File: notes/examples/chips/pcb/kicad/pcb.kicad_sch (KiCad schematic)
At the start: 12 parts, among them J1 BOOT, J2 UART, SW1 BOOT, SW2 USER, U1 STM32F103C8Tx, U2 AMS1117-3.3

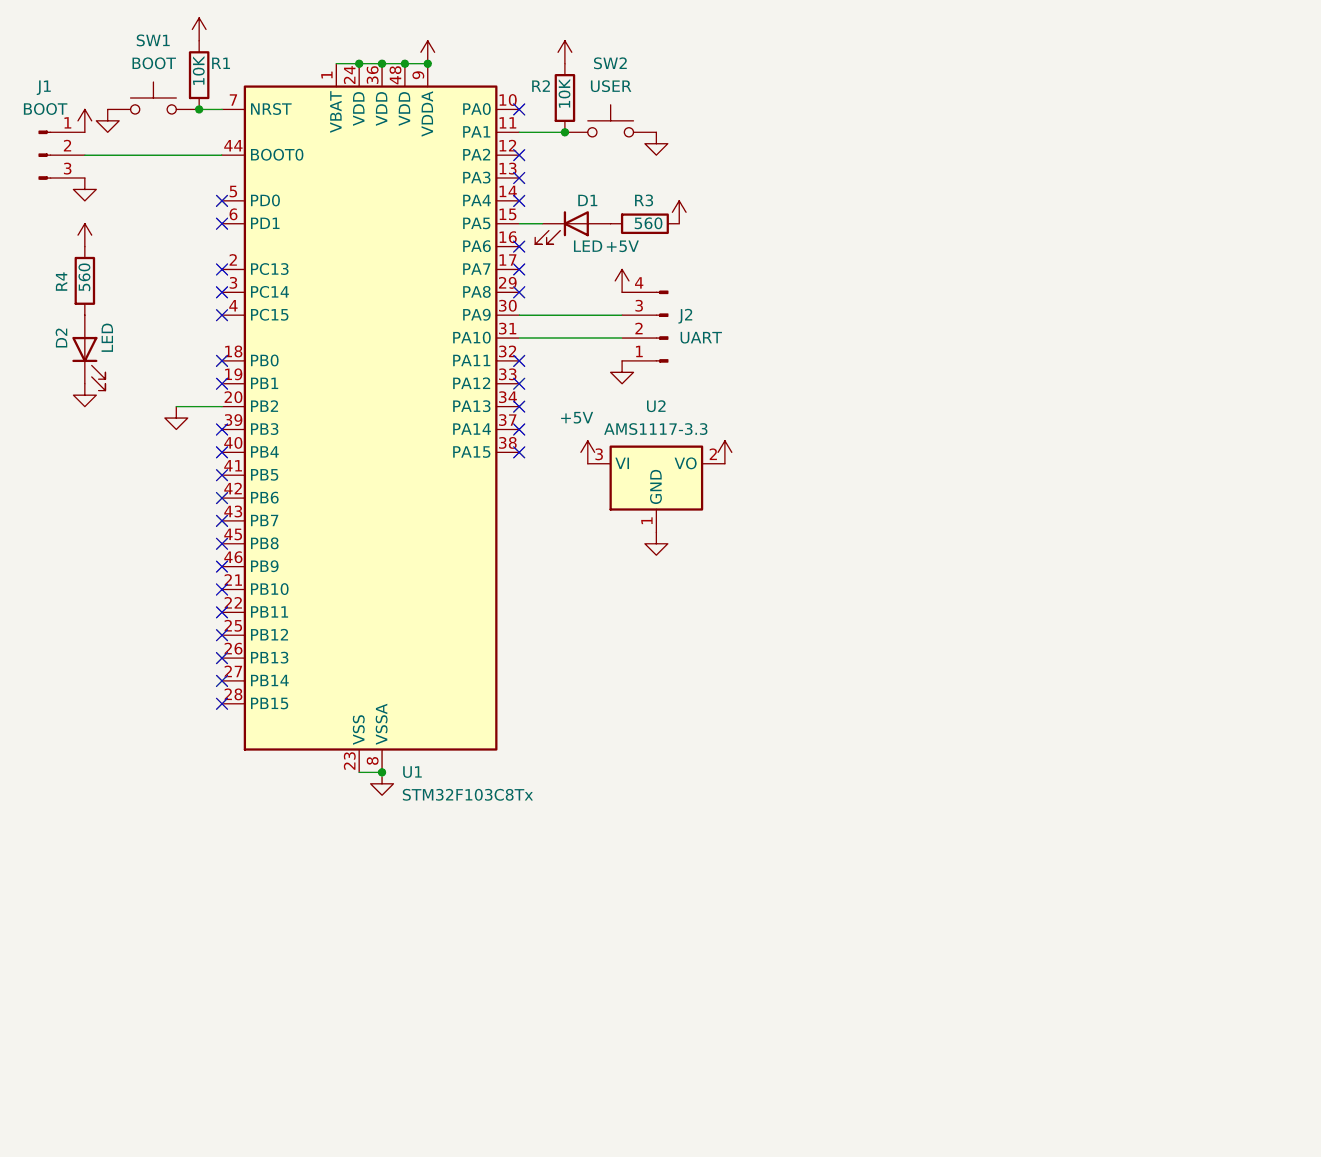
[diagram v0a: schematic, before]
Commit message: Rework KiCAD Guide
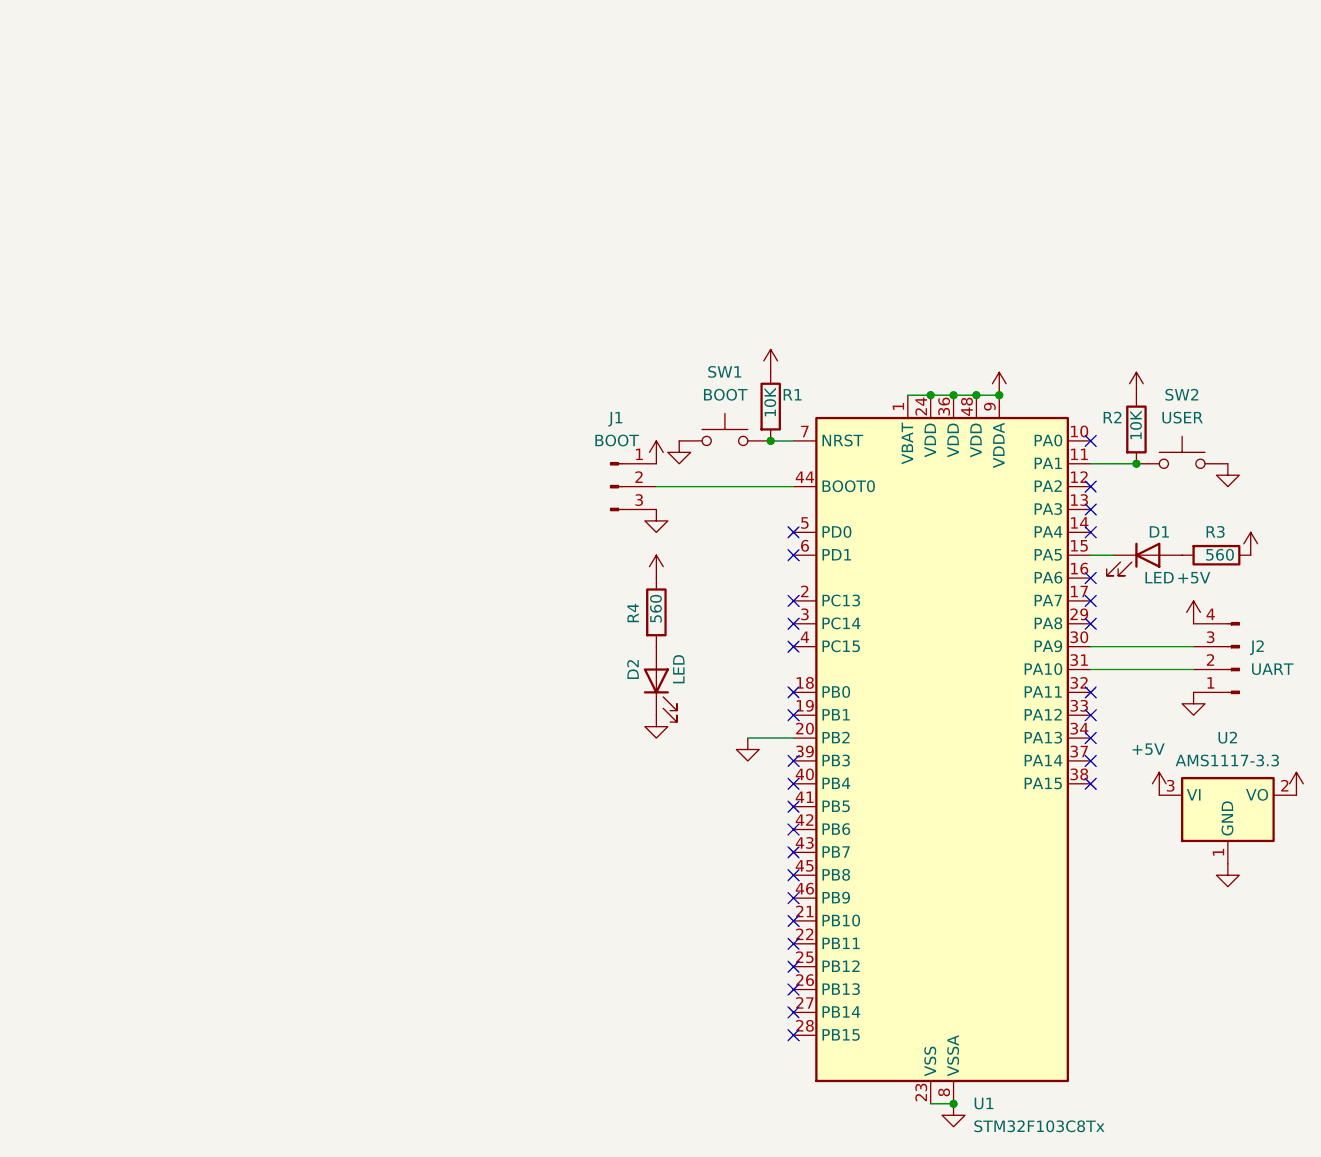
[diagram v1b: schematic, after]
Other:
- moved on the sheet: D1, D2, J1, J2, R1, R2, R3, R4, SW1, SW2, U1, U2
